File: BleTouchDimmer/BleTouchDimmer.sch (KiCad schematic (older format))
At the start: 14 parts, among them P1 PROG, P2 UART, P3 POWER, U2 MDBT40, Y2 Crystal

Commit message: Finished power supply and protection circuit, connected all sheets.
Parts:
- added R?: PTCC, symbol RVAR
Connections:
- net labels added: 230_VAC_L, N, TR1_CTRL, TR1_L_OUT, TR2_CTRL, TR2_L_OUT
- net labels removed: N_IN
- wire segments 59 -> 77
- no-connect marks 27 -> 25
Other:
- note added: "POWER AND TRIACS"
- note added: "TODO\nENCODER/TOUCHWHEEL\nBACKUP BAT"
- note removed: "TODO\nPOWERSUPPLY\nPROTECTION\nENCODER/TOUCHWHEEL"
- moved on the sheet: C3, C4, C7, C9, P3, R1, R4, U2, VR?

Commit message: Started cap sensor logic.
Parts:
- gave numbers to parts that had none: 2
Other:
- note added: "TODO\nENCODER/TOUCHWHEEL\nBACKUP BAT??"
- note removed: "TODO\nENCODER/TOUCHWHEEL\nBACKUP BAT"
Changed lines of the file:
@@
 NoConn ~ 7000 2650
 NoConn ~ 7000 2950
-NoConn ~ 7000 3050
-NoConn ~ 7000 3150
 NoConn ~ 4600 3000
 NoConn ~ 4600 2900
@@
 $EndSheet
 $Comp
-L VR VR?
+L VR VR1
 U 1 1 582F67C7
 P 2200 4700
-F 0 "VR?" V 2260 4654 50  0000 C TNN
+F 0 "VR1" V 2260 4654 50  0000 C TNN
 F 1 "VR" V 2200 4700 50  0000 C CNN
 F 2 "Varistors:RV_Disc_D9_W4.4_P5" H 2200 4700 50  0001 C CNN
@@
 N
 $Comp
-L RVAR R?
+L RVAR R22
 U 1 1 582F5F6C
 P 1800 4400
-F 0 "R?" V 1880 4350 50  0000 C CNN
+F 0 "R22" V 1880 4350 50  0000 C CNN
 F 1 "PTCC" V 1700 4450 50  0000 C CNN
 F 2 "" H 1800 4400 50  0000 C CNN
@@
 Wire Wire Line
 	4350 6550 4950 6550
-Wire Wire Line
-	5800 3550 5800 4250
-Wire Wire Line
-	5900 3550 5900 4250
 Text Label 4950 6400 2    60   ~ 0
 TR1_CTRL
 Text Label 4950 6550 2    60   ~ 0
 TR2_CTRL
-Text Label 5800 4250 1    60   ~ 0
+Text Label 7700 3150 2    60   ~ 0
 TR1_CTRL
-Text Label 5900 4250 1    60   ~ 0
+Text Label 7700 3050 2    60   ~ 0
 TR2_CTRL
 Wire Wire Line
@@
 POWER AND TRIACS
 Text Notes 650  850  0    60   Italic 12
-TODO\nENCODER/TOUCHWHEEL\nBACKUP BAT
+TODO\nENCODER/TOUCHWHEEL\nBACKUP BAT??
+Wire Wire Line
+	7000 3150 7700 3150
+Wire Wire Line
+	7000 3050 7700 3050
+NoConn ~ 5800 3550
+NoConn ~ 5900 3550
 $EndSCHEMATC

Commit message: Uncommited changes.
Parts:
- C3, C4, C7, C9: footprint Capacitors_SMD:C_0805 -> Capacitors_SMD:C_0603
- D1: footprint Resistors_SMD:R_0603_HandSoldering -> LEDs:LED_0603; symbol LED -> LED-RESCUE-BleTouchDimmer
- R1, R3, R4: footprint Resistors_SMD:R_0805 -> Resistors_SMD:R_0603
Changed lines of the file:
@@
 EESchema Schematic File Version 2
+LIBS:BleTouchDimmer-rescue
+LIBS:cypress_touch
+LIBS:azoteq_touch
 LIBS:power
 LIBS:device
@@
 LIBS:Symbols_Microcontroller_Philips-NXP_RevA_06Oct2013
 LIBS:nordicsemi
-LIBS:Egert
 LIBS:Oscillators
 LIBS:74xgxx
@@
 LIBS:microchip_pic16mcu
 LIBS:microchip_pic18mcu
-LIBS:microchip_pic32mcu
 LIBS:motor_drivers
 LIBS:motors
@@
 LIBS:SymbolsSimilarEN60617+oldDIN617-RevE8
 LIBS:BleTouchDimmer-cache
-EELAYER 25 0
+EELAYER 26 0
 EELAYER END
 $Descr A4 11693 8268
@@
 F 0 "C3" H 3625 3200 50  0000 L CNN
 F 1 "22pF" H 3625 3000 50  0000 L CNN
-F 2 "Capacitors_SMD:C_0805" H 3638 2950 50  0001 C CNN
+F 2 "Capacitors_SMD:C_0603" H 3638 2950 50  0001 C CNN
 F 3 "" H 3600 3100 50  0000 C CNN
 	1    3600 3100
@@
 F 0 "C4" H 3625 2650 50  0000 L CNN
 F 1 "22pF" H 3625 2450 50  0000 L CNN
-F 2 "Capacitors_SMD:C_0805" H 3638 2400 50  0001 C CNN
+F 2 "Capacitors_SMD:C_0603" H 3638 2400 50  0001 C CNN
 F 3 "" H 3600 2550 50  0000 C CNN
 	1    3600 2550
@@
 F 0 "C9" H 3625 2200 50  0000 L CNN
 F 1 "1u" H 3625 2000 50  0000 L CNN
-F 2 "Capacitors_SMD:C_0805" H 3638 1950 50  0001 C CNN
+F 2 "Capacitors_SMD:C_0603" H 3638 1950 50  0001 C CNN
 F 3 "" H 3600 2100 50  0000 C CNN
 	1    3600 2100
@@
 F 0 "C7" H 5225 4750 50  0000 L CNN
 F 1 "1u" H 5225 4550 50  0000 L CNN
-F 2 "Capacitors_SMD:C_0805" H 5238 4500 50  0001 C CNN
+F 2 "Capacitors_SMD:C_0603" H 5238 4500 50  0001 C CNN
 F 3 "" H 5200 4650 50  0000 C CNN
 	1    5200 4650
@@
 F 0 "R1" V 8080 2700 50  0000 C CNN
 F 1 "10k" V 8000 2700 50  0000 C CNN
-F 2 "Resistors_SMD:R_0805" V 7930 2700 50  0001 C CNN
+F 2 "Resistors_SMD:R_0603" V 7930 2700 50  0001 C CNN
 F 3 "" H 8000 2700 50  0000 C CNN
 	1    8000 2700
@@
 F 0 "R3" V 9080 4700 50  0000 C CNN
 F 1 "10k" V 9000 4700 50  0000 C CNN
-F 2 "Resistors_SMD:R_0805" V 8930 4700 50  0001 C CNN
+F 2 "Resistors_SMD:R_0603" V 8930 4700 50  0001 C CNN
 F 3 "" H 9000 4700 50  0000 C CNN
 	1    9000 4700
@@
 F 0 "R4" V 7180 3500 50  0000 C CNN
 F 1 "100R" V 7100 3500 50  0000 C CNN
-F 2 "Resistors_SMD:R_0805" V 7030 3500 50  0001 C CNN
+F 2 "Resistors_SMD:R_0603" V 7030 3500 50  0001 C CNN
 F 3 "" H 7100 3500 50  0000 C CNN
 	1    7100 3500
@@
 $EndComp
 $Comp
-L LED D1
+L LED-RESCUE-BleTouchDimmer D1
 U 1 1 581F1C9A
 P 7100 3950
 F 0 "D1" H 7100 4050 50  0000 C CNN
 F 1 "LED" H 7100 3850 50  0000 C CNN
-F 2 "Resistors_SMD:R_0603_HandSoldering" H 7100 3950 50  0001 C CNN
+F 2 "LEDs:LED_0603" H 7100 3950 50  0001 C CNN
 F 3 "" H 7100 3950 50  0000 C CNN
 	1    7100 3950

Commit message: Started changing controller to esp32-wroom module.
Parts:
- removed C3, C4: 22pF, Capacitors_SMD:C_0603, symbol C
- removed C9: 1u, Capacitors_SMD:C_0603, symbol C
- removed Y2: Crystal, EgertKiCad_lib:Crystal_ECX-31B, symbol Crystal
- added C?: 100n, Capacitors_SMD:C_0603, symbol C
- added C?: 10u, Capacitors_SMD:C_0603, symbol C
- added R?: 10k, Resistors_SMD:R_0603, symbol R
- added U6: ESP32-WROOM, esp_library:ESP32-WROOM, symbol ESP32-WROOM
- C7: value 1u -> 100n
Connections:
- net labels added: TOUCH0, TOUCH1, TOUCH2, TOUCH3, TOUCH4, TOUCH5, TOUCH6, TOUCH7, TOUCH8, TOUCH9
- wire segments 77 -> 82
- no-connect marks 25 -> 48
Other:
- moved on the sheet: C7, D1, R1, R4, U2

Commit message: Updated schematic.
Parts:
- removed C?: 100n, Capacitors_SMD:C_0603, symbol C
- removed P1: PROG, Socket_Strips:Socket_Strip_Straight_1x04, symbol CONN_01X04
- removed P2: UART, Socket_Strips:Socket_Strip_Straight_1x04, symbol CONN_01X04
- removed R?: 10k, Resistors_SMD:R_0603, symbol R
- removed U2: MDBT40, EgertKiCad_lib:MDBT40, symbol MDBT40
- added C3: 1n, Capacitors_SMD:C_0603, symbol C
- added J1, J2: Conn_01x03, Connectors_Molex:Molex_SPOX-5267_22-03-5035_03x2.54mm_Straight, symbol Conn_01x03
- added J3: JTAG, Connectors_Molex:Molex_SPOX-5267_22-03-5075_07x2.54mm_Straight, symbol Conn_01x07
- added J4: Conn_01x06, Connectors_Molex:Molex_SPOX-5267_22-03-5065_06x2.54mm_Straight, symbol Conn_01x06
- added J5: SLIDER1, Connectors_Molex:Molex_SPOX-5267_22-03-5055_05x2.54mm_Straight, symbol Conn_01x05
- added J6: SLIDER2, Connectors_Molex:Molex_SPOX-5267_22-03-5055_05x2.54mm_Straight, symbol Conn_01x05
- added Q3, Q4: PDTC123J, TO_SOT_Packages_SMD:SOT-23, symbol DTC123J
- added Q5, Q6: BC850, TO_SOT_Packages_SMD:SOT-23, symbol BC850
- added R2: 100R, Resistors_SMD:R_0603, symbol R
- added R23, R24, R25, R26: 0R, Resistors_SMD:R_0603, symbol R
- added R27, R28: 2k2, Resistors_SMD:R_0603, symbol R
- added R29: 10k, Resistors_SMD:R_0603, symbol R
- added SW1: SW_PUSH, Buttons_Switches_SMD:SW_SPST_B3SL-1022P, symbol SW_PUSH
- R1: value 10k -> 100R
- gave numbers to parts that had none: 1
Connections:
- net TOUCH9 is gone; now on net TR2_CTRL: U6.8 (IO32)
- net +3V3: now also C1.1, C7.1, R1.1, U6.2 (3V3), J3.1 (Pin_1), J4.1 (Pin_1), R2.1, R29.2
- net GND: now also C3.1, J1.1 (Pin_1), J2.1 (Pin_1), J3.7 (Pin_7), J4.6 (Pin_6), J5.5 (Pin_5), J6.5 (Pin_5), Q3.2 (E), Q4.2 (E), SW1.2; no longer R1.1
- net RX: now also U6.34 (RXD0), J4.2 (Pin_2)
- net TOUCH0: now also J5.4 (Pin_4)
- net TOUCH2: now also J5.3 (Pin_3)
- net TOUCH7: now also J5.2 (Pin_2)
- net TOUCH8: now also J5.1 (Pin_1)
- net TR1_CTRL: now also U6.7 (IO35)
- net TX: now also U6.35 (TXD0), J4.3 (Pin_3)
- net ZC_DETECT: now also U6.6 (IO34)
- net DEBUG_LED: now reaches R4.2
- net DEBUG_LED: now also U6.4 (SENSOR_VP)
- net LED1: now reaches U6.10 (IO25)
- net LED1: now also Q3.1 (B)
- net LED2: now reaches U6.11 (IO26)
- net LED2: now also Q4.1 (B)
- net RESET: now reaches U6.3 (EN)
- net RESET: now also C3.2, J3.6 (Pin_6), Q5.3 (C), R29.1, SW1.1
- net SWDCLK: no longer names the net of R1.2
- net SWDCLK: now also J1.3 (Pin_3)
- net TOUCH1 renamed BOOT
- net BOOT: now also Q6.3 (C)
- net TOUCH3 renamed TOUCH3/MTDO
- net TOUCH3/MTDO: now also J6.4 (Pin_4), R26.1
- net TOUCH4 renamed TOUCH4/MTCK
- net TOUCH4/MTCK: now also J6.3 (Pin_3), R25.1
- net TOUCH5 renamed TOUCH5/MTDI
- net TOUCH5/MTDI: now also J6.2 (Pin_2), R24.1
- net TOUCH6 renamed TOUCH6/MTMS
- net TOUCH6/MTMS: now also J6.1 (Pin_1), R23.1
- new net: Q5.1 (B), R27.1
- new net: Q6.1 (B), R28.1
- new net: J3.2 (Pin_2), R23.2
- new net: J3.3 (Pin_3), R24.2
- new net: J3.4 (Pin_4), R25.2
- new net: J3.5 (Pin_5), R26.2
- new net: J1.2 (Pin_2), Q3.3 (C)
- new net: J2.2 (Pin_2), Q4.3 (C)
- new net: J2.3 (Pin_3), R2.2
- new net DTR: J4.5 (Pin_5), Q6.2 (E), R27.2
- new net RTS: J4.4 (Pin_4), Q5.2 (E), R28.2
- no-connect marks 48 -> 16
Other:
- note added: "RESET"
- note added: "UART/PROG"
- note removed: "PROG/DEBUG"
- note removed: "UART"
- moved on the sheet: D1, R4

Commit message: Started placing footprints on pcb. Maybe needs to split pcb to power part and controller part.
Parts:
- R22: footprint (none) -> Varistors:RV_Disc_D7_W5.5_P5
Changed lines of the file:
@@
-EESchema Schematic File Version 3
+EESchema Schematic File Version 2
 LIBS:BleTouchDimmer-rescue
+LIBS:cypress_touch
+LIBS:azoteq_touch
 LIBS:power
 LIBS:device
+LIBS:transistors
+LIBS:conn
 LIBS:linear
 LIBS:regul
+LIBS:74xx
+LIBS:cmos4000
 LIBS:adc-dac
 LIBS:memory
@@
 LIBS:digital-audio
 LIBS:philips
+LIBS:display
 LIBS:cypress
 LIBS:siliconi
@@
 LIBS:atmel
 LIBS:contrib
-LIBS:Espressif
+LIBS:valves
+LIBS:Symbols_Microcontroller_Philips-NXP_RevA_06Oct2013
+LIBS:nordicsemi
+LIBS:Egert
+LIBS:Oscillators
 LIBS:ac-dc
 LIBS:Altera
 LIBS:analog_devices
+LIBS:battery_management
+LIBS:bbd
+LIBS:brooktre
+LIBS:dc-dc
+LIBS:diode
+LIBS:elec-unifil
+LIBS:ESD_Protection
+LIBS:ftdi
+LIBS:gennum
+LIBS:graphic
+LIBS:hc11
+LIBS:ir
+LIBS:Lattice
+LIBS:maxim
+LIBS:microchip_dspic33dsc
+LIBS:microchip_pic10mcu
+LIBS:microchip_pic12mcu
+LIBS:microchip_pic16mcu
+LIBS:microchip_pic18mcu
+LIBS:microchip_pic32mcu
+LIBS:motor_drivers
+LIBS:nxp_armmcu
+LIBS:onsemi
+LIBS:Power_Management
+LIBS:powerint
+LIBS:pspice
+LIBS:references
+LIBS:rfcom
+LIBS:sensors
+LIBS:silabs
+LIBS:supertex
+LIBS:video
+LIBS:wiznet
+LIBS:Worldsemi
+LIBS:Xicor
+LIBS:Zilog
+LIBS:Symbols_DCDC-ACDC-Converter_RevC_20Jul2012
+LIBS:Symbols_EN60617_13Mar2013
+LIBS:Symbols_EN60617-10_HF-Radio_DRAFT_12Sep2013
+LIBS:Symbols_ICs-Diskrete_RevD10
+LIBS:Symbols_ICs-Opto_RevB_16Sep2013
+LIBS:Symbols_Socket-DIN41612_RevA
+LIBS:Symbols_Transformer-Diskrete_RevA
+LIBS:SymbolsSimilarEN60617+oldDIN617-RevE8
+LIBS:Espressif
+LIBS:ESP32-footprints-Shem-Lib
+LIBS:espressif-xess
 LIBS:Battery_Management
-LIBS:bbd
 LIBS:bosch
-LIBS:brooktre
 LIBS:Connector
-LIBS:dc-dc
 LIBS:Diode
 LIBS:Display
 LIBS:driver_gate
 LIBS:DSP_Microchip_DSPIC33
-LIBS:elec-unifil
-LIBS:ESD_Protection
 LIBS:FPGA_Actel
-LIBS:ftdi
-LIBS:gennum
 LIBS:Graphic
-LIBS:hc11
 LIBS:infineon
 LIBS:intersil
-LIBS:ir
-LIBS:Lattice
 LIBS:LED
 LIBS:LEM
@@
 LIBS:logic_programmable
 LIBS:Logic_TTL_IEEE
-LIBS:maxim
 LIBS:MCU_Microchip_PIC10
 LIBS:MCU_Microchip_PIC12
@@
 LIBS:modules
 LIBS:Motor
-LIBS:motor_drivers
-LIBS:nordicsemi
 LIBS:nxp
-LIBS:onsemi
-LIBS:Oscillators
-LIBS:powerint
-LIBS:Power_Management
-LIBS:pspice
-LIBS:references
 LIBS:Relay
-LIBS:rfcom
 LIBS:RFSolutions
 LIBS:Sensor_Current
-LIBS:sensors
-LIBS:silabs
-LIBS:supertex
 LIBS:Switch
 LIBS:Transformer
@@
 LIBS:triac_thyristor
 LIBS:Valve
-LIBS:video
-LIBS:wiznet
-LIBS:Worldsemi
-LIBS:Xicor
 LIBS:zetex
-LIBS:Zilog
 LIBS:BleTouchDimmer-cache
-EELAYER 26 0
+EELAYER 25 0
 EELAYER END
 $Descr A4 11693 8268
@@
 $EndComp
 $Comp
-L GND #PWR06
+L GND #PWR7
 U 1 1 581A884C
 P 3150 1500
-F 0 "#PWR06" H 3150 1250 50  0001 C CNN
+F 0 "#PWR7" H 3150 1250 50  0001 C CNN
 F 1 "GND" H 3150 1350 50  0000 C CNN
 F 2 "" H 3150 1500 50  0000 C CNN
@@
 $EndComp
 $Comp
-L +3.3V #PWR08
+L +3.3V #PWR9
 U 1 1 581AC6F3
 P 4400 850
-F 0 "#PWR08" H 4400 700 50  0001 C CNN
+F 0 "#PWR9" H 4400 700 50  0001 C CNN
 F 1 "+3.3V" H 4400 990 50  0000 C CNN
 F 2 "" H 4400 850 50  0000 C CNN
@@
 TX
 $Comp
-L GND #PWR013
+L GND #PWR21
 U 1 1 581EB2A9
 P 10000 5350
-F 0 "#PWR013" H 10000 5100 50  0001 C CNN
+F 0 "#PWR21" H 10000 5100 50  0001 C CNN
 F 1 "GND" H 10000 5200 50  0000 C CNN
 F 2 "" H 10000 5350 50  0000 C CNN
@@
 $EndComp
 $Comp
-L +3.3V #PWR014
+L +3.3V #PWR18
 U 1 1 581EB479
 P 9200 4750
-F 0 "#PWR014" H 9200 4600 50  0001 C CNN
+F 0 "#PWR18" H 9200 4600 50  0001 C CNN
 F 1 "+3.3V" H 9200 4890 50  0000 C CNN
 F 2 "" H 9200 4750 50  0000 C CNN
@@
 $EndComp
 $Comp
-L +3.3V #PWR015
+L +3.3V #PWR17
 U 1 1 581EE473
 P 9000 4500
-F 0 "#PWR015" H 9000 4350 50  0001 C CNN
+F 0 "#PWR17" H 9000 4350 50  0001 C CNN
 F 1 "+3.3V" H 9000 4640 50  0000 C CNN
 F 2 "" H 9000 4500 50  0000 C CNN
@@
 $EndComp
 $Comp
-L GND #PWR016
+L GND #PWR8
 U 1 1 581F1D57
 P 3850 2600
-F 0 "#PWR016" H 3850 2350 50  0001 C CNN
+F 0 "#PWR8" H 3850 2350 50  0001 C CNN
 F 1 "GND" H 3850 2450 50  0000 C CNN
 F 2 "" H 3850 2600 50  0000 C CNN
@@
 ZC_DETECT
 $Comp
-L PWR_FLAG #FLG017
+L PWR_FLAG #FLG1
 U 1 1 581FAA9C
 P 10450 850
-F 0 "#FLG017" H 10450 945 50  0001 C CNN
+F 0 "#FLG1" H 10450 945 50  0001 C CNN
 F 1 "PWR_FLAG" H 10450 1030 50  0000 C CNN
 F 2 "" H 10450 850 50  0000 C CNN
@@
 $EndComp
 $Comp
-L GND #PWR018
+L GND #PWR23
 U 1 1 581FAAED
 P 10450 1150
-F 0 "#PWR018" H 10450 900 50  0001 C CNN
+F 0 "#PWR23" H 10450 900 50  0001 C CNN
 F 1 "GND" H 10450 1000 50  0000 C CNN
 F 2 "" H 10450 1150 50  0000 C CNN
@@
 $EndComp
 $Comp
-L +3.3V #PWR019
+L +3.3V #PWR24
 U 1 1 581FAB37
 P 10800 850
-F 0 "#PWR019" H 10800 700 50  0001 C CNN
+F 0 "#PWR24" H 10800 700 50  0001 C CNN
 F 1 "+3.3V" H 10800 990 50  0000 C CNN
 F 2 "" H 10800 850 50  0000 C CNN
@@
 $EndComp
 $Comp
-L PWR_FLAG #FLG020
+L PWR_FLAG #FLG2
 U 1 1 581FAB81
 P 10800 1100
-F 0 "#FLG020" H 10800 1195 50  0001 C CNN
+F 0 "#FLG2" H 10800 1195 50  0001 C CNN
 F 1 "PWR_FLAG" H 10800 1280 50  0000 C CNN
 F 2 "" H 10800 1100 50  0000 C CNN
@@
 F 0 "R22" V 1880 4350 50  0000 C CNN
 F 1 "PTCC" V 1700 4450 50  0000 C CNN
-F 2 "" H 1800 4400 50  0000 C CNN
+F 2 "Varistors:RV_Disc_D7_W5.5_P5" H 1800 4400 50  0001 C CNN
 F 3 "http://www.mouser.com/ds/2/427/ptccl265vseries-109202.pdf" H 1800 4400 50  0001 C CNN
 F 4 "http://www.mouser.ee/ProductDetail/Vishay/PTCCL05H630HBE/?qs=%2fha2pyFaduhe5MnjzSnUuqgECKBNFzw%252bCXjAzFqnpFOVPihHyum5eg%3d%3d" V 1800 4400 60  0001 C CNN "Ordering"
@@
 NoConn ~ 5100 1750
 $Comp
-L GND #PWR010
+L GND #PWR11
 U 1 1 59F4B047
 P 5500 3150
-F 0 "#PWR010" H 5500 2900 50  0001 C CNN
+F 0 "#PWR11" H 5500 2900 50  0001 C CNN
 F 1 "GND" H 5500 3000 50  0000 C CNN
 F 2 "" H 5500 3150 50  0000 C CNN
@@
 $EndComp
 $Comp
-L GND #PWR09
+L GND #PWR10
 U 1 1 59F4BF69
 P 5050 2800
-F 0 "#PWR09" H 5050 2550 50  0001 C CNN
+F 0 "#PWR10" H 5050 2550 50  0001 C CNN
 F 1 "GND" H 5050 2650 50  0000 C CNN
 F 2 "" H 5050 2800 50  0000 C CNN
@@
 $EndComp
 $Comp
-L GND #PWR011
+L GND #PWR14
 U 1 1 59F4BFDA
 P 7000 2750
-F 0 "#PWR011" H 7000 2500 50  0001 C CNN
+F 0 "#PWR14" H 7000 2500 50  0001 C CNN
 F 1 "GND" H 7000 2600 50  0000 C CNN
 F 2 "" H 7000 2750 50  0000 C CNN
@@
 $EndComp
 $Comp
-L +3.3V #PWR020
+L +3.3V #PWR19
 U 1 1 59F4DFEE
 P 9800 2250
-F 0 "#PWR020" H 9800 2100 50  0001 C CNN
+F 0 "#PWR19" H 9800 2100 50  0001 C CNN
 F 1 "+3.3V" H 9800 2390 50  0000 C CNN
 F 2 "" H 9800 2250 50  0000 C CNN
@@
 $EndComp
 $Comp
-L GND #PWR024
+L GND #PWR22
 U 1 1 59F4E008
 P 10050 3700
-F 0 "#PWR024" H 10050 3450 50  0001 C CNN
+F 0 "#PWR22" H 10050 3450 50  0001 C CNN
 F 1 "GND" H 10050 3550 50  0000 C CNN
 F 2 "" H 10050 3700 50  0000 C CNN
@@
 $EndComp
 $Comp
-L GND #PWR023
+L GND #PWR20
 U 1 1 59F4E011
 P 9800 3450
-F 0 "#PWR023" H 9800 3200 50  0001 C CNN
+F 0 "#PWR20" H 9800 3200 50  0001 C CNN
 F 1 "GND" H 9800 3300 50  0000 C CNN
 F 2 "" H 9800 3450 50  0000 C CNN
@@
 Connection ~ 4400 950
 $Comp
-L +3.3V #PWR012
+L +3.3V #PWR15
 U 1 1 59F5B99A
 P 8550 3050
-F 0 "#PWR012" H 8550 2900 50  0001 C CNN
+F 0 "#PWR15" H 8550 2900 50  0001 C CNN
 F 1 "+3.3V" H 8550 3190 50  0000 C CNN
 F 2 "" H 8550 3050 50  0000 C CNN
@@
 	8550 3150 8550 3050
 $Comp
-L GND #PWR017
+L GND #PWR16
 U 1 1 59F5BC57
 P 8550 3800
-F 0 "#PWR017" H 8550 3550 50  0001 C CNN
+F 0 "#PWR16" H 8550 3550 50  0001 C CNN
 F 1 "GND" H 8550 3650 50  0000 C CNN
 F 2 "" H 8550 3800 50  0000 C CNN
@@
 $EndComp
 $Comp
-L GND #PWR04
+L GND #PWR4
 U 1 1 59F61F36
 P 2000 2300
-F 0 "#PWR04" H 2000 2050 50  0001 C CNN
+F 0 "#PWR4" H 2000 2050 50  0001 C CNN
 F 1 "GND" H 2000 2150 50  0000 C CNN
 F 2 "" H 2000 2300 50  0000 C CNN
@@
 $EndComp
 $Comp
-L +3V3 #PWR03
+L +3V3 #PWR3
 U 1 1 59F61F4D
 P 2000 1400
-F 0 "#PWR03" H 2000 1250 50  0001 C CNN
+F 0 "#PWR3" H 2000 1250 50  0001 C CNN
 F 1 "+3V3" H 2000 1540 50  0000 C CNN
 F 2 "" H 2000 1400 50  0000 C CNN
@@
 $EndComp
 $Comp
-L GND #PWR07
+L GND #PWR6
 U 1 1 59F63694
 P 2000 3650
-F 0 "#PWR07" H 2000 3400 50  0001 C CNN
+F 0 "#PWR6" H 2000 3400 50  0001 C CNN
 F 1 "GND" H 2000 3500 50  0000 C CNN
 F 2 "" H 2000 3650 50  0000 C CNN
@@
 $EndComp
 $Comp
-L +3V3 #PWR05
+L +3V3 #PWR5
 U 1 1 59F636A2
 P 2000 2750
-F 0 "#PWR05" H 2000 2600 50  0001 C CNN
+F 0 "#PWR5" H 2000 2600 50  0001 C CNN
 F 1 "+3V3" H 2000 2890 50  0000 C CNN
 F 2 "" H 2000 2750 50  0000 C CNN
@@
 $EndComp
 $Comp
-L GND #PWR02
+L GND #PWR2
 U 1 1 59F672E9
 P 1600 3350
-F 0 "#PWR02" H 1600 3100 50  0001 C CNN
+F 0 "#PWR2" H 1600 3100 50  0001 C CNN
 F 1 "GND" H 1600 3200 50  0000 C CNN
 F 2 "" H 1600 3350 50  0000 C CNN
@@
 $EndComp
 $Comp
-L GND #PWR01
+L GND #PWR1
 U 1 1 59F67368
 P 1600 2000
-F 0 "#PWR01" H 1600 1750 50  0001 C CNN
+F 0 "#PWR1" H 1600 1750 50  0001 C CNN
 F 1 "GND" H 1600 1850 50  0000 C CNN
 F 2 "" H 1600 2000 50  0000 C CNN
@@
 $EndComp
 $Comp
-L GND #PWR025
+L GND #PWR12
 U 1 1 59F687EF
 P 5700 4550
-F 0 "#PWR025" H 5700 4300 50  0001 C CNN
+F 0 "#PWR12" H 5700 4300 50  0001 C CNN
 F 1 "GND" H 5700 4400 50  0000 C CNN
 F 2 "" H 5700 4550 50  0000 C CNN
@@
 $EndComp
 $Comp
-L GND #PWR038
+L GND #PWR13
 U 1 1 59F6899E
 P 5700 5350
-F 0 "#PWR038" H 5700 5100 50  0001 C CNN
+F 0 "#PWR13" H 5700 5100 50  0001 C CNN
 F 1 "GND" H 5700 5200 50  0000 C CNN
 F 2 "" H 5700 5350 50  0000 C CNN

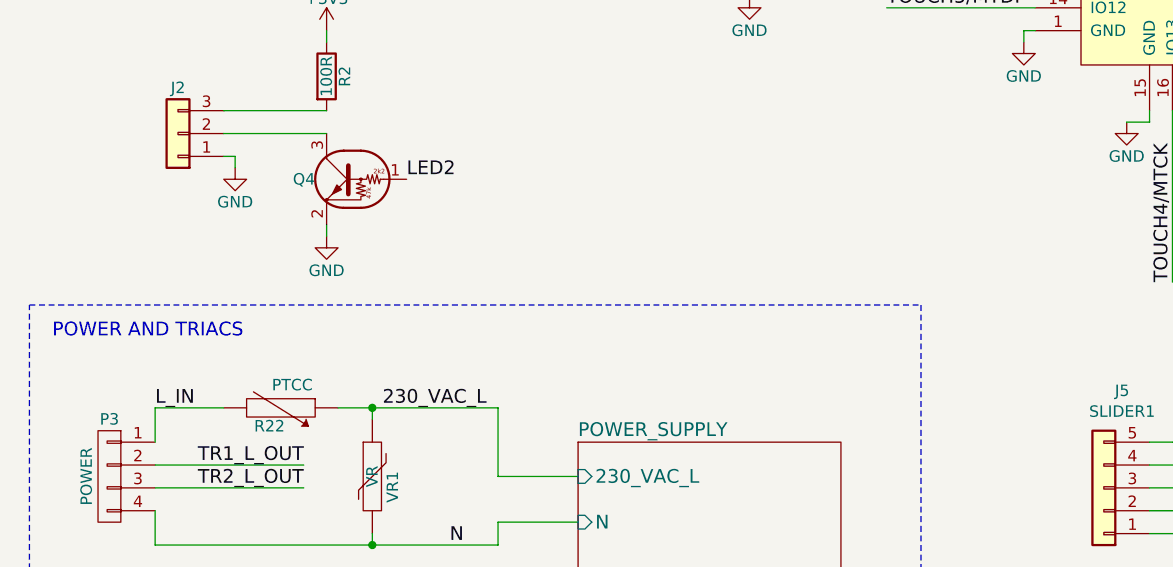
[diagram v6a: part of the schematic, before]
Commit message: Added comment about cheaper terminal block solution.
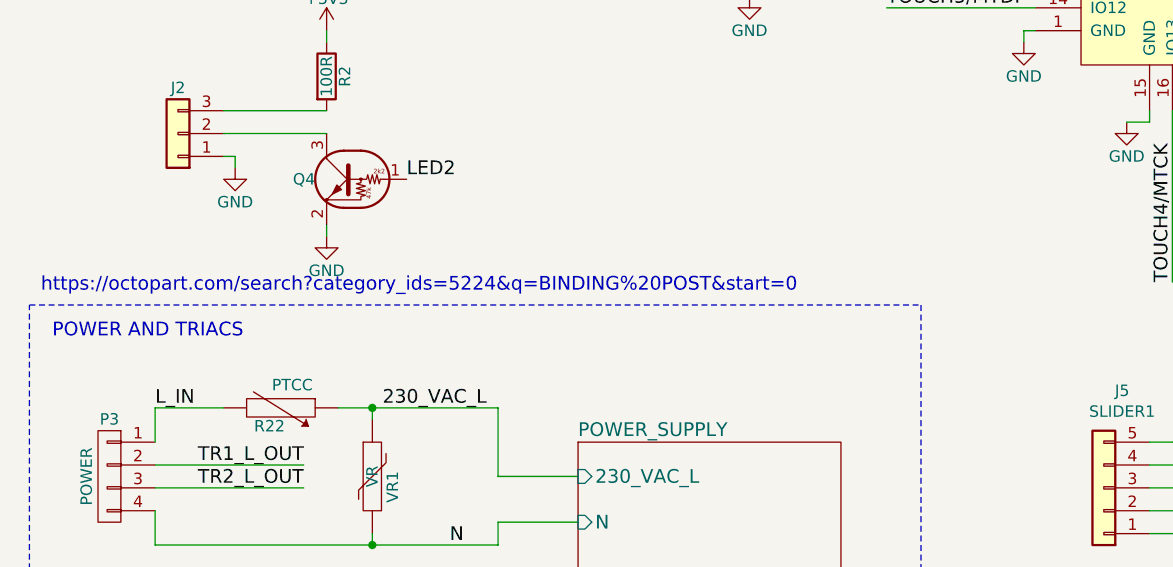
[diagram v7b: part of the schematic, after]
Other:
- note added: "https://octopart.com/search?category_ids=5224&q=BINDING%20POST&start=0"
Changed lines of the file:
@@
 Text Label 8000 5450 0    60   ~ 0
 BOOT
+Text Notes 750  3900 0    60   ~ 0
+https://octopart.com/search?category_ids=5224&q=BINDING%20POST&start=0
 $EndSCHEMATC
